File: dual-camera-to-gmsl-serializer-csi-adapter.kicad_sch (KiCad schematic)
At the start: 19 parts, among them J1 Conn_FFC_WE_68715014022, J2 Conn_FFC_WE_68715014022, J3 Conn_FFC_WE_68715014022, U1 TPS2117DRLR, U2 AP62301_TSOT

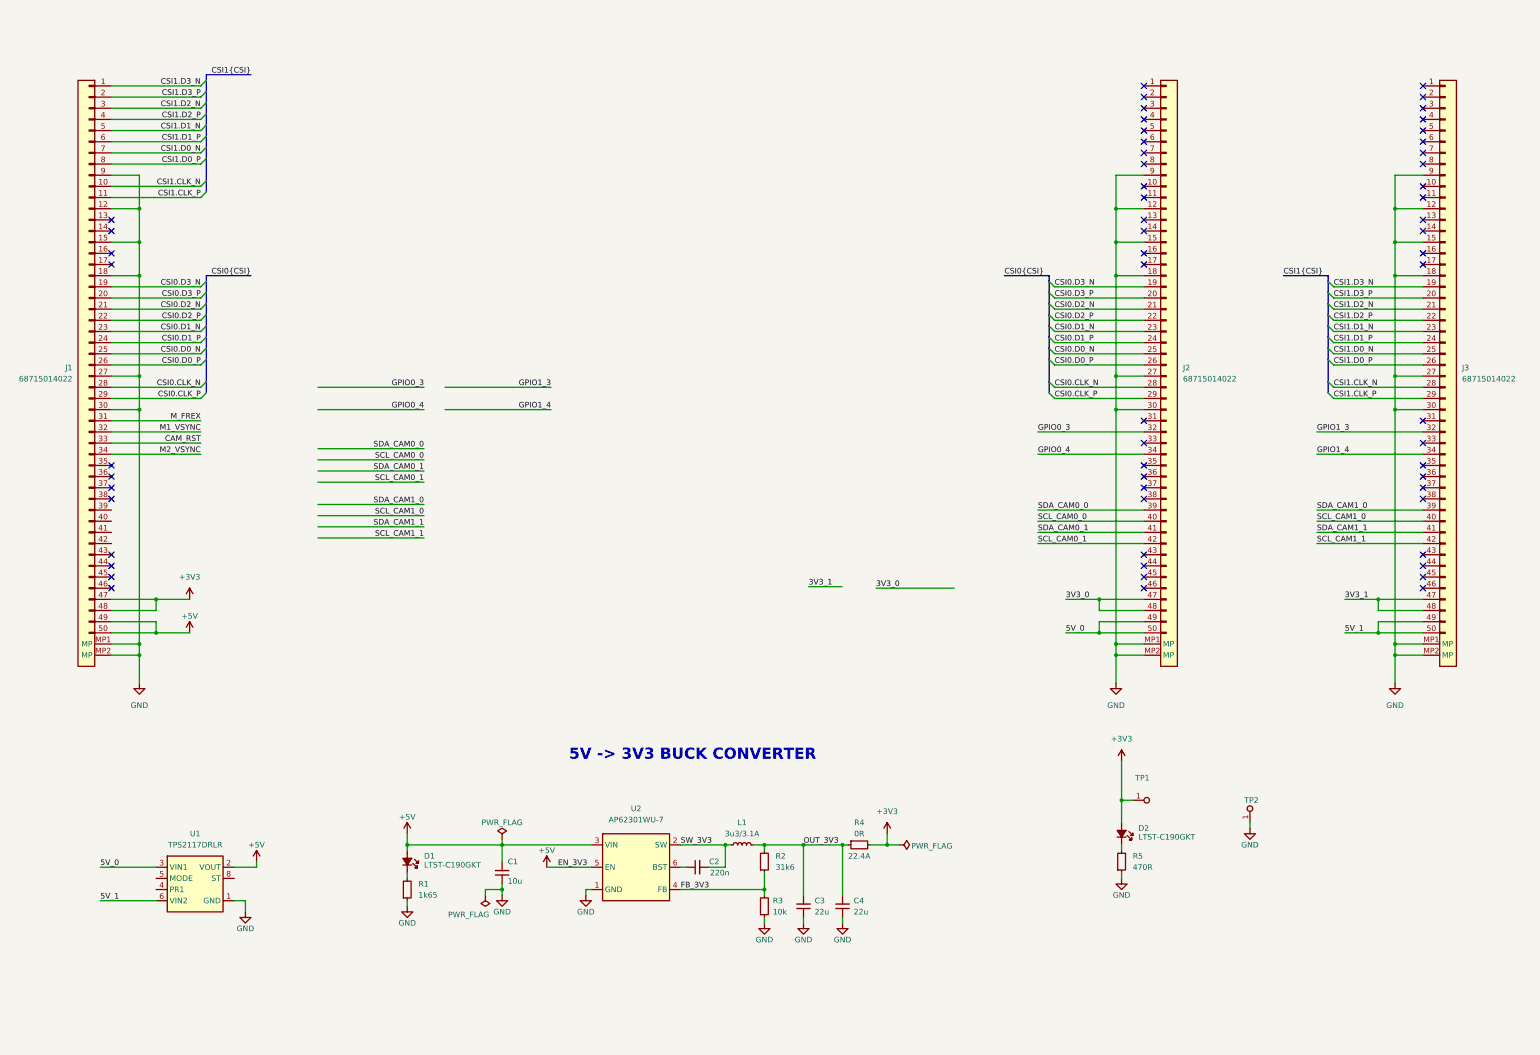
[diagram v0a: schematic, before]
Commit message: [#69172] Add resistor selectors
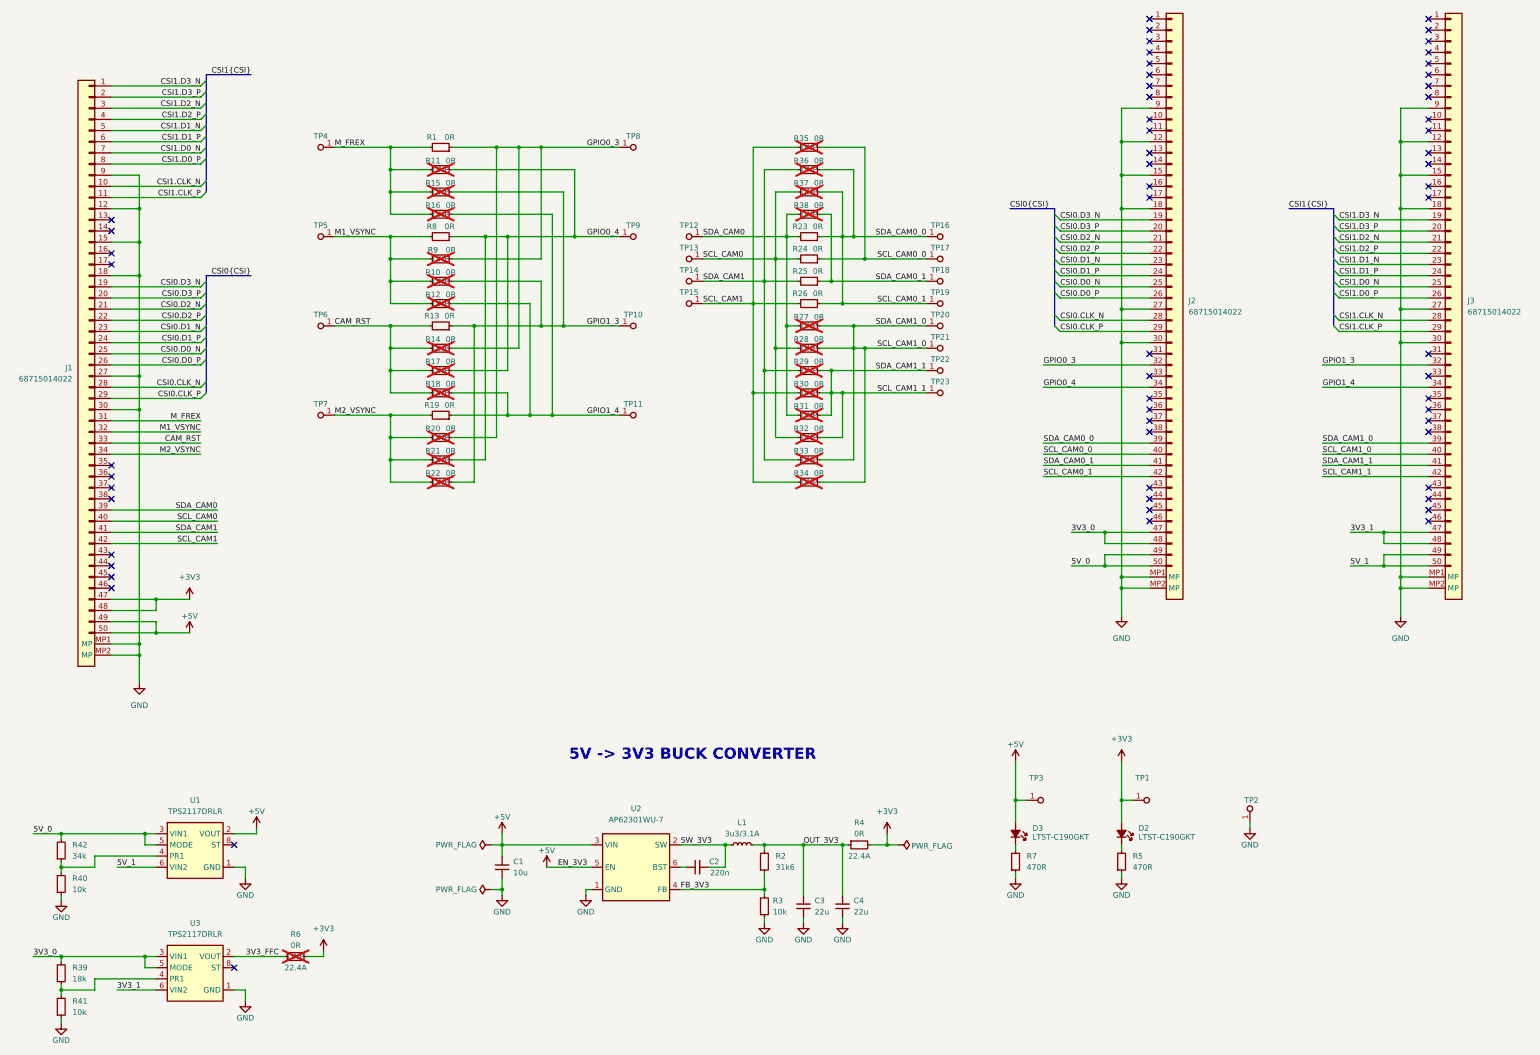
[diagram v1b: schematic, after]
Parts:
- removed D1: LED_G_0603_LTST-C190GKT, antmicro-footprints:LED_0603_1608Metric_G, symbol antmicroLEDIndicationDiscrete:LED_G_0603_LTST-C190GKT
- removed R1: R_1k65_0402, antmicro-footprints:R_0402_1005Metric, symbol antmicroResistors0402:R_1k65_0402
- added D3: LED_G_0603_LTST-C190GKT, antmicro-footprints:LED_0603_1608Metric_G, symbol antmicroLEDIndicationDiscrete:LED_G_0603_LTST-C190GKT
- added R1, R10, R11, R12, R13, R14, R15, R16, R17, R18, R19, R20, R21, R22, R23, R24, R25, R26, R27, R28, R29, R30, R31, R32, R33, R34, R35, R36, R37, R38, R8, R9: R_0R_0402, antmicro-footprints:R_0402_1005Metric, symbol Resistors0402:R_0R_0402
- added R39: R_18k_0402, antmicro-footprints:R_0402_1005Metric, symbol Resistors0402:R_18k_0402
- added R40, R41: R_10k_0402, antmicro-footprints:R_0402_1005Metric, symbol Resistors0402:R_10k_0402
- added R42: R_34k_0402, antmicro-footprints:R_0402_1005Metric, symbol Resistors0402:R_34k_0402
- added R6: R_0R_22.4A_0603, antmicro-footprints:R_0603_1608Metric, symbol antmicroResistors0603:R_0R_22.4A_0603
- added R7: R_470R_0402, antmicro-footprints:R_0402_1005Metric, symbol antmicroResistors0402:R_470R_0402
- added TP10, TP11, TP12, TP13, TP14, TP15, TP16, TP17, TP18, TP19, TP20, TP21, TP22, TP23, TP3, TP4, TP5, TP6, TP7, TP8, TP9: TP_1.5mm_SMD, antmicro-footprints:TP_SMD_1.5mm, symbol antmicroTestPoints:TP_1.5mm_SMD
- added U3: TPS2117DRLR, antmicro-footprints:SOT-583, symbol PMICPowerDistributionSwitchesLoadDrivers:TPS2117DRLR
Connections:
- net SDA_CAM0_0 is gone; now on net SCL_CAM0_1: J2.39
- net SDA_CAM1_0 is gone; now on net SCL_CAM1_0: J3.39
- net SDA_CAM1_1 is gone; now on net SCL_CAM1_1: J3.41
- net +3V3: now also R6.2
- net +5V: now also D3.2 (A), TP3.1
- net 3V3_0: now also R39.2, U3.3 (VIN1), U3.5 (MODE)
- net 3V3_1: now also U3.6 (VIN2)
- net 5V_0: now also U1.5 (MODE), R42.2
- net CAM_RST: now also R13.2, R14.2, R17.2, R18.2, TP6.1
- net GND: now also R40.1, R41.1, R7.1, U3.1 (GND)
- net GPIO0_3: now also R1.1, R14.1, R20.1, R9.1, TP8.1
- net GPIO0_4: now also R11.1, R17.1, R21.1, R8.1, TP9.1
- net GPIO1_3: now also R10.1, R13.1, R15.1, R22.1, TP10.1
- net GPIO1_4: now also R12.1, R16.1, R18.1, R19.1, TP11.1
- net M1_VSYNC: now also R10.2, R12.2, R8.2, R9.2, TP5.1
- net M2_VSYNC: now also R19.2, R20.2, R21.2, R22.2, TP7.1
- net M_FREX: now also R1.2, R11.2, R15.2, R16.2, TP4.1
- net SCL_CAM0_0: now also R24.1, R35.1, TP17.1
- net SCL_CAM0_1: now also R23.1, R26.1, R36.1, R37.1, TP16.1, TP19.1
- net SCL_CAM1_0: now also R27.1, R28.1, R33.1, R34.1, TP20.1, TP21.1
- net SCL_CAM1_1: now also R29.1, R30.1, R31.1, R32.1, TP22.1, TP23.1
- net SDA_CAM0_1: now also R25.1, R38.1, TP18.1
- net at U1.4 (PR1): now also R40.2, R42.1
- net SDA_CAM0: now reaches J1.39
- net SDA_CAM0: now also R23.2, R27.2, R31.2, R38.2, TP12.1
- net SCL_CAM0: now reaches J1.40
- net SCL_CAM0: now also R24.2, R28.2, R32.2, R37.2, TP13.1
- net SDA_CAM1: now reaches J1.41
- net SDA_CAM1: now also R25.2, R29.2, R33.2, R36.2, TP14.1
- net SCL_CAM1: now reaches J1.42
- net SCL_CAM1: now also R26.2, R30.2, R34.2, R35.2, TP15.1
- new net: D3.1 (C), R7.2
- new net: R39.1, R41.2, U3.4 (PR1)
- new net 3V3_FFC: R6.1, U3.2 (VOUT), U3.7 (VOUT)
- no-connect marks 60 -> 62
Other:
- moved on the sheet: C1, J2, J3, U1

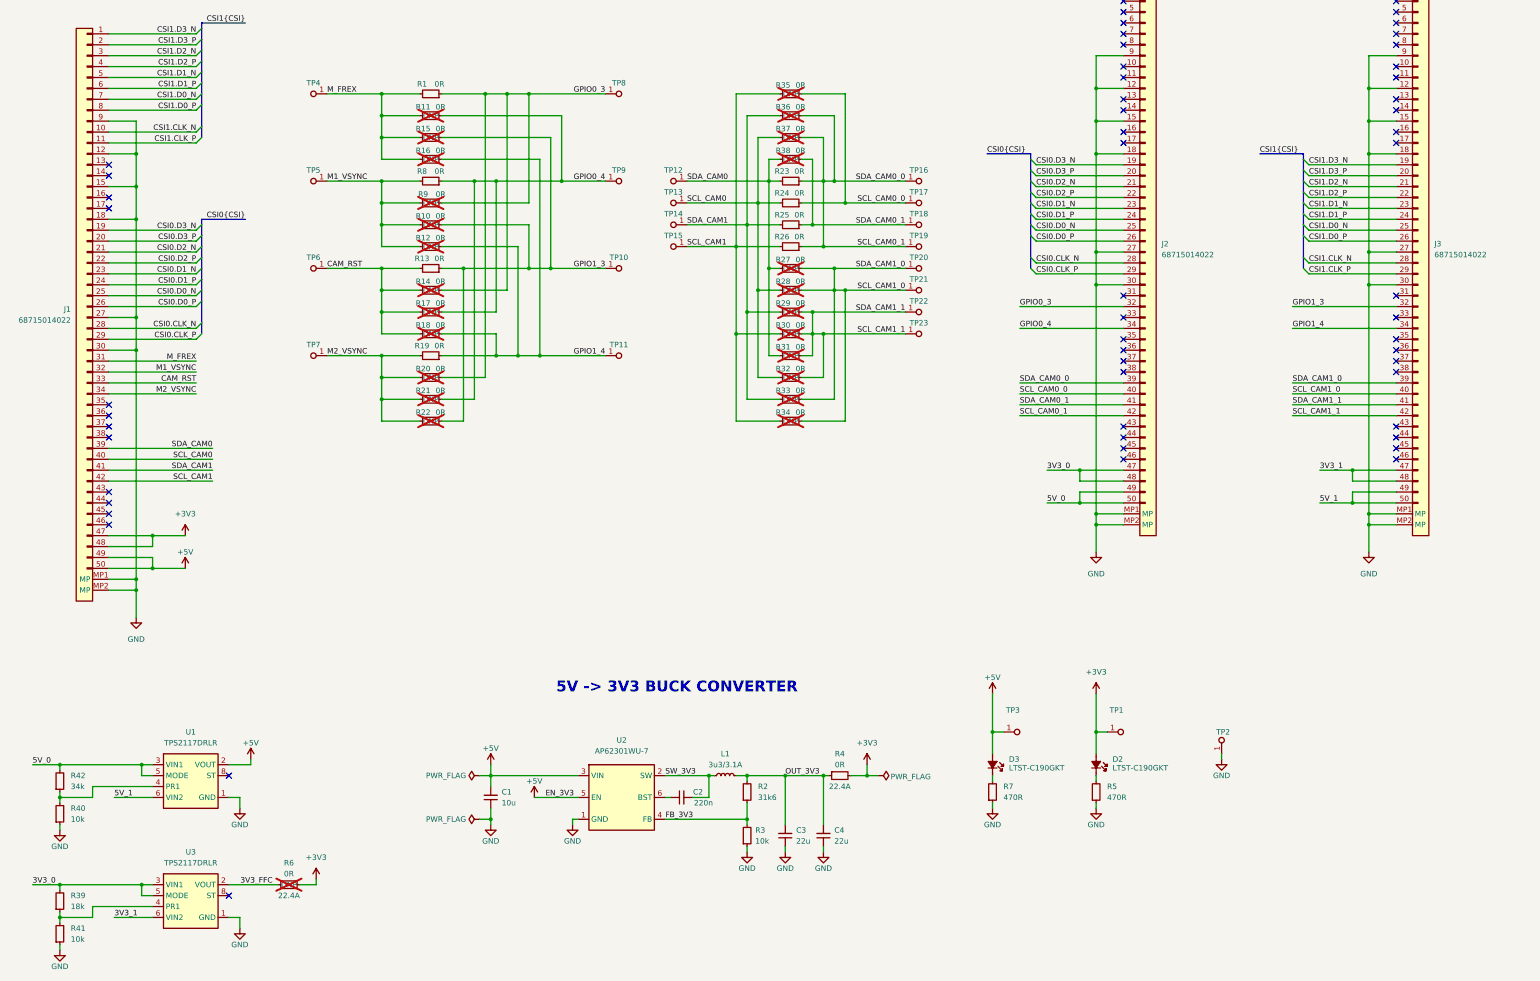
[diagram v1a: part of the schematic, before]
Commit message: [#69172] Transfer schematic onto pcb
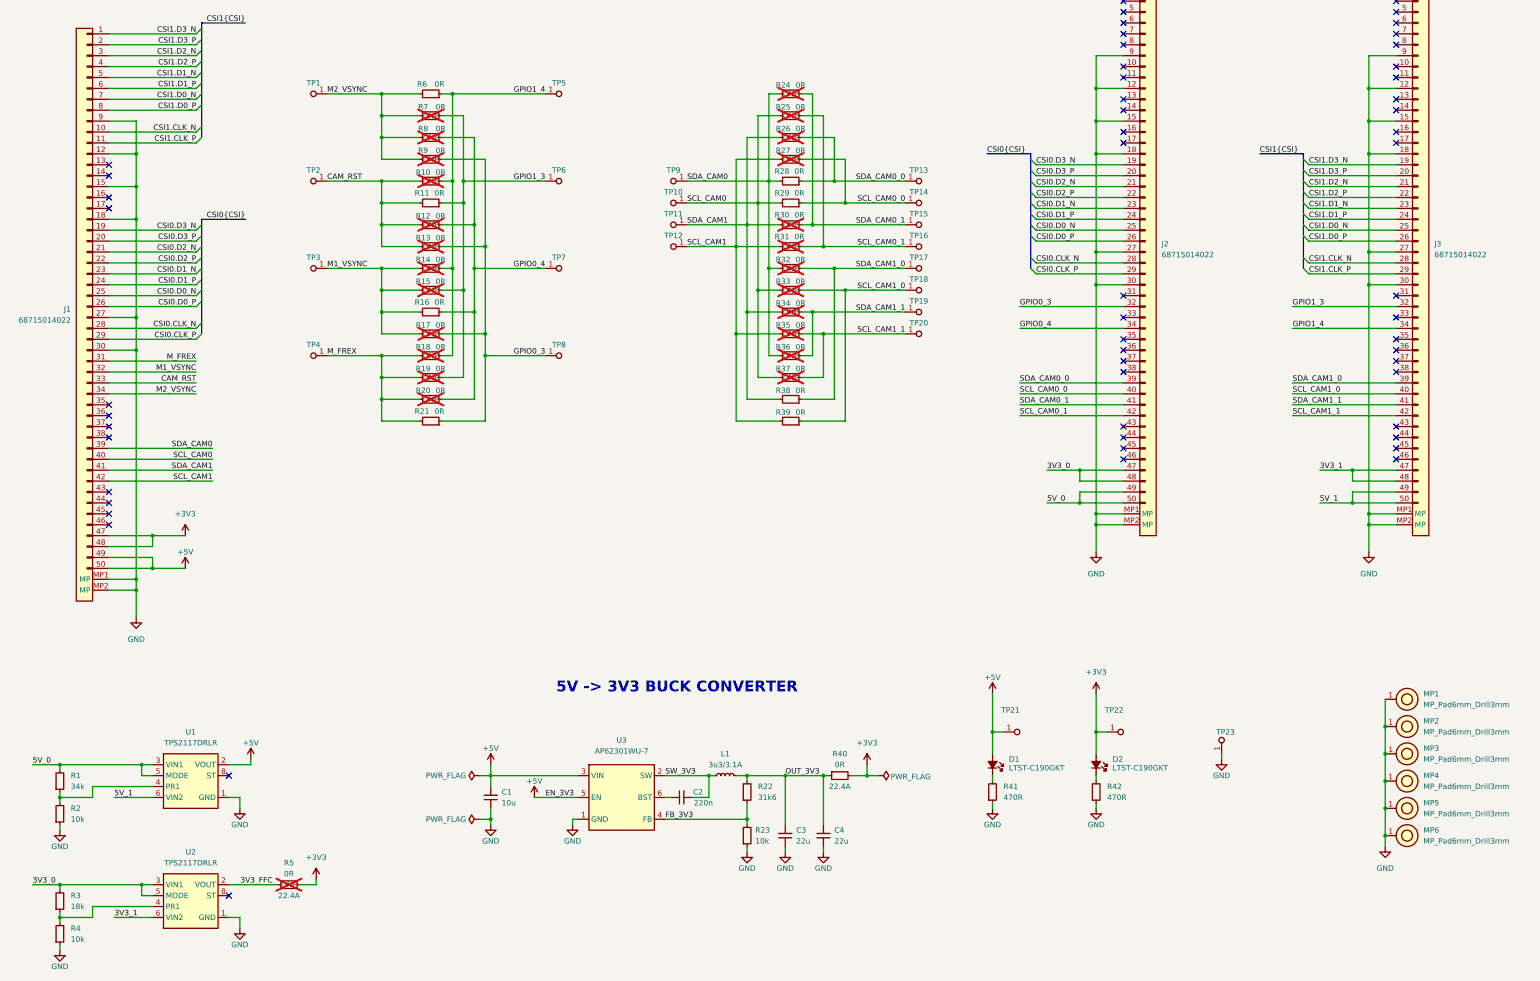
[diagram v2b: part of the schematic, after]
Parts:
- removed R12, R17, R22, R8, R9: R_0R_0402, antmicro-footprints:R_0402_1005Metric, symbol Resistors0402:R_0R_0402
- added MP1, MP2, MP3, MP4, MP5, MP6: MP_Pad6mm_Drill3mm, antmicro-footprints:MP_Pad6mm_Drill3mm, symbol MechanicalParts:MP_Pad6mm_Drill3mm
- added R10, R11, R15, R16, R18: R_0R_0402, antmicro-footprints:R_0402_1005Metric, symbol Resistors0402:R_0R_0402
- R13, R19: DNP (none) -> DNP; now not fitted; now left out of the parts list
- R21: DNP DNP -> (none); now fitted; now in the parts list
- R30: renamed from R25; DNP (none) -> DNP; now not fitted; now left out of the parts list
- R31: renamed from R26; DNP (none) -> DNP; now not fitted
- R38: renamed from R33; DNP DNP -> (none); now fitted; now in the parts list
- R39: renamed from R34; DNP DNP -> (none); now fitted; now in the parts list
- renumbered D3 to D1, R42 to R1, R10 to R12, R18 to R17, R40 to R2, R2 to R22, R3 to R23, R38 to R24, R37 to R25, R36 to R26, R35 to R27, R23 to R28, R24 to R29, R39 to R3, R27 to R32, R28 to R33, R29 to R34, R30 to R35, R31 to R36, R32 to R37, R41 to R4, R4 to R40, R7 to R41, R5 to R42, R6 to R5, R1 to R6, R11 to R7, R15 to R8, R16 to R9, TP4 to TP1, TP13 to TP10, TP14 to TP11, TP15 to TP12, TP16 to TP13, TP17 to TP14, TP18 to TP15, TP19 to TP16, TP20 to TP17, TP21 to TP18, TP22 to TP19, TP5 to TP2, TP23 to TP20, TP3 to TP21, TP1 to TP22, TP2 to TP23, TP6 to TP3, TP7 to TP4, TP8 to TP5, TP9 to TP6, TP10 to TP7, TP11 to TP8, TP12 to TP9, U3 to U2, U2 to U3
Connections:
- net CAM_RST: now also R12.2, TP2.1, R10.2, R11.2; no longer R14.2, R17.2, TP3.1
- net GND: now also MP1.1, MP2.1, MP3.1, MP4.1, MP5.1, MP6.1
- net GPIO0_3: now also R13.1, R17.1, R21.1, R9.1, TP8.1; no longer R14.1, R20.1, R6.1, TP5.1
- net GPIO0_4: now also R12.1, R20.1, R8.1, TP7.1, R16.1; no longer R21.1, R7.1, TP6.1
- net GPIO1_3: now also R19.1, R7.1, TP6.1, R11.1, R15.1; no longer R12.1, R13.1, R8.1, TP7.1
- net GPIO1_4: now also R14.1, R6.1, TP5.1, R10.1, R18.1; no longer R17.1, R19.1, R9.1, TP8.1
- net M1_VSYNC: now also R14.2, R17.2, TP3.1, R15.2, R16.2; no longer R12.2, TP2.1
- net M2_VSYNC: now also R6.2, R7.2, R8.2, R9.2, TP1.1; no longer R19.2, R20.2, R21.2, TP4.1
- net M_FREX: now also R19.2, R20.2, R21.2, TP4.1, R18.2; no longer R6.2, R7.2, R8.2, R9.2, TP1.1
- net SCL_CAM0_1: no longer J2.39, R26.1, R28.1, TP13.1
- net SCL_CAM1_0: no longer J3.39, R32.1, R38.1, TP17.1
- net SCL_CAM1_1: no longer J3.41, R34.1, R36.1, TP19.1
- new net SDA_CAM0_0: J2.39, R26.1, R28.1, TP13.1
- new net SDA_CAM1_0: J3.39, R32.1, R38.1, TP17.1
- new net SDA_CAM1_1: J3.41, R34.1, R36.1, TP19.1
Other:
- moved on the sheet: R24, R25, R26, R27, TP5, TP6, TP7, TP8

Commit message: [#69172] Update schematics
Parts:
- removed MP1, MP2, MP3, MP4, MP5, MP6: MP_Pad6mm_Drill3mm, antmicro-footprints:MP_Pad6mm_Drill3mm, symbol MechanicalParts:MP_Pad6mm_Drill3mm
- removed R1: R_34k_0402, antmicro-footprints:R_0402_1005Metric, symbol Resistors0402:R_34k_0402
- removed R11, R13, R15, R17, R19, R21, R7, R9: R_0R_0402, antmicro-footprints:R_0402_1005Metric, symbol Resistors0402:R_0R_0402
- removed R2, R4: R_10k_0402, antmicro-footprints:R_0402_1005Metric, symbol Resistors0402:R_10k_0402
- removed R3: R_18k_0402, antmicro-footprints:R_0402_1005Metric, symbol Resistors0402:R_18k_0402
- removed R42: R_470R_0402, antmicro-footprints:R_0402_1005Metric, symbol antmicroResistors0402:R_470R_0402
- added C10, C5, C6, C7, C8, C9: C_100n_0402, antmicro-footprints:C_0402_1005Metric, symbol Capacitors0402:C_100n_0402
- added D3, D4, D5, D6: LED_G_0603_LTST-C190GKT, antmicro-footprints:LED_0603_1608Metric_G, symbol LEDIndicationDiscrete:LED_G_0603_LTST-C190GKT
- added H1, H2, H3, H4, H5, H6, H7, H8: Spacer_Drill3.7mm_H3mm_9774030151R, antmicro-footprints:Spacer_Drill3.7mm_H3mm_9774030151R, symbol MechanicalParts:Spacer_Drill3.7mm_H3mm_9774030151R
- added R1, R3: R_470R_0402, antmicro-footprints:R_0402_1005Metric, symbol Resistors0402:R_470R_0402
- added R11, R13, R15, R17, R19, R21, R7, R9: R_10k_0402, antmicro-footprints:R_0402_1005Metric, symbol Resistors0402:R_10k_0402
- added R2, R4, R42: R_200R_0402, antmicro-footprints:R_0402_1005Metric, symbol Resistors0402:R_200R_0402
- added R43, R44: R_12k_0402, antmicro-footprints:R_0402_1005Metric, symbol Resistors0402:R_12k_0402
- added R45, R46: R_0R_0402, antmicro-footprints:R_0402_1005Metric, symbol Resistors0402:R_0R_0402
- added TP24, TP25, TP26, TP27: TP_1.5mm_SMD, antmicro-footprints:TP_SMD_1.5mm, symbol TestPoints:TP_1.5mm_SMD
- C1: symbol antmicroCapacitors0603:C_10u_25V_0603 -> Capacitors0603:C_10u_25V_0603
- C2: symbol antmicroCapacitors0402:C_220n_0402 -> Capacitors0402:C_220n_0402
- C3, C4: symbol antmicroCapacitors0402:C_22u_0402 -> Capacitors0402:C_22u_0402
- D1, D2: symbol antmicroLEDIndicationDiscrete:LED_G_0603_LTST-C190GKT -> LEDIndicationDiscrete:LED_G_0603_LTST-C190GKT
- L1: symbol antmicroFixedInductors:L_3u3_3.1A_Bourns-SRP3212A -> FixedInductors:L_3u3_3.1A_Bourns-SRP3212A
- R23: symbol antmicroResistors0402:R_10k_0402 -> Resistors0402:R_10k_0402
- R40: symbol antmicroResistors0603:R_0R_22.4A_0603 -> Resistors0603:R_0R_22.4A_0603
- R41: symbol antmicroResistors0402:R_470R_0402 -> Resistors0402:R_470R_0402
- R5: symbol antmicroResistors0603:R_0R_22.4A_0603 -> Resistors0603:R_0R_22.4A_0603; now in the parts list
- TP1, TP10, TP11, TP12, TP13, TP14, TP15, TP16, TP17, TP18, TP19, TP2, TP20, TP21, TP22, TP23, TP3, TP4, TP5, TP6, TP7, TP8, TP9: symbol antmicroTestPoints:TP_1.5mm_SMD -> TestPoints:TP_1.5mm_SMD
- U3: symbol antmicroDCDCConverters:AP62301_TSOT -> DCDCConverters:AP62301_TSOT
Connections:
- net +3V3: now also C5.2
- net +5V: now also C6.2, R45.2; no longer U3.5 (EN)
- net 3V3_0: now also C7.2, D4.2 (A), TP25.1; no longer U2.5 (MODE)
- net 3V3_1: now also C9.2, D6.2 (A), TP27.1
- net 5V_0: now also C8.2, D3.2 (A), TP24.1; no longer U1.5 (MODE)
- net 5V_1: now also C10.2, D5.2 (A), TP26.1
- net CAM_RST: now also R11.1, R13.1
- net GND: now also U1.4 (PR1), U1.5 (MODE), U2.4 (PR1), U2.5 (MODE), C10.1, C5.1, C6.1, C7.1, C8.1, C9.1, H1.1, H2.1, H3.1, H4.1, H5.1, H6.1, H7.1, H8.1, R1.1, R2.1, R3.1, R4.1, R42.1, R43.1, R44.1, R46.2
- net GPIO0_3: now also R13.2, R17.2, R21.2, R44.2, R9.2
- net GPIO1_3: now also R11.2, R15.2, R19.2, R43.2, R7.2
- net M1_VSYNC: now also R15.1, R17.1
- net M2_VSYNC: now also R7.1, R9.1
- net M_FREX: now also R19.1, R21.1
- net at D2.1 (C): now also R2.2
- new net: D4.1 (C), R4.2
- new net: D3.1 (C), R1.2
- new net: D5.1 (C), R3.2
- new net: D6.1 (C), R42.2
- new net EN_3V3: R45.1, R46.1, U3.5 (EN)
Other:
- note added: "5V -> 3V3 Buck Converter"
- note added: "Dual Camera Connector"
- note added: "GMSL Serializer Board Connector 1"
- note added: "GMSL Serializer Board Connector 2"
- note added: "GPIO Selector Resistors"
- note added: "I2C Selector Resistors"
- note added: "Mounting studs"
- note added: "Power Arbiters"
- note added: "Power Status LEDs"
- note removed: "5V -> 3V3 BUCK CONVERTER"
- company: (none) -> Antmicro Ltd
- title: (none) -> Dual Camera to GMSL Serializer CSI Adapter
- moved on the sheet: C1, C2, C3, C4, D1, D2, J1, J2, J3, L1, R10, R12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
